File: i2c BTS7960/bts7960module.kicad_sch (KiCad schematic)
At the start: 42 parts, among them J2 Conn_01x04, J5 jst, U10 BTS7960B, U11 BTS7960B, U7 74AHC244, U8 BTS7960B, U9 BTS7960B

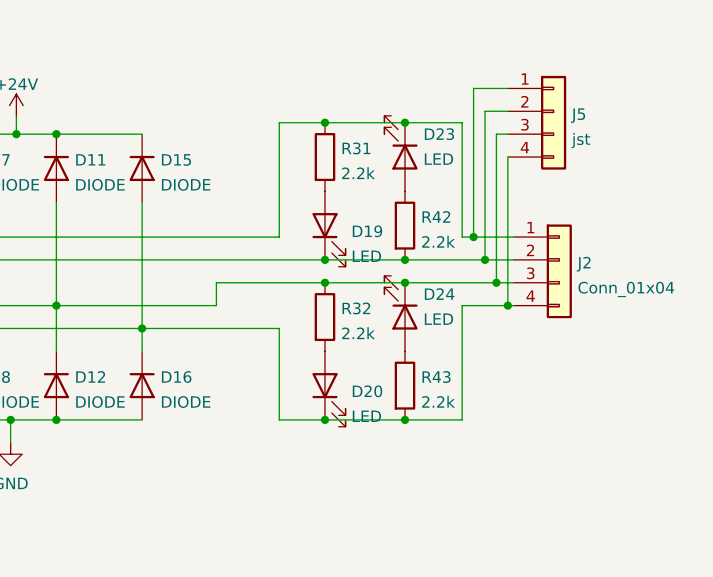
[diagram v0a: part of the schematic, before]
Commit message: tweaked buck converter hole sizes and silk
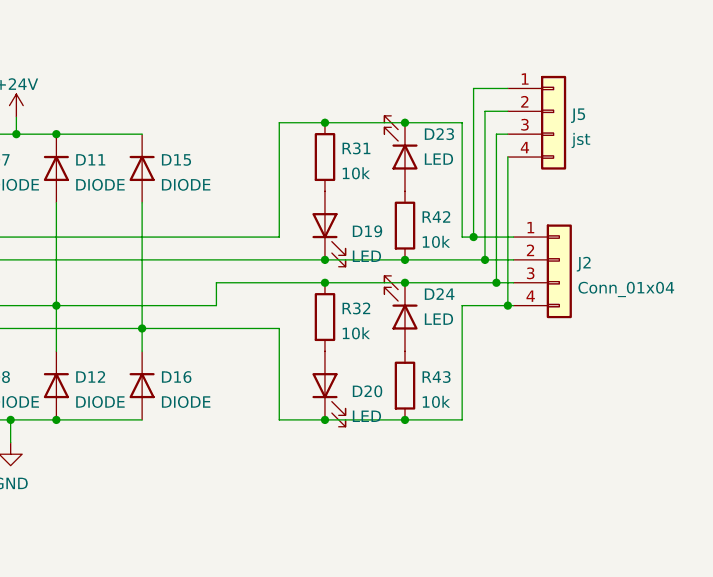
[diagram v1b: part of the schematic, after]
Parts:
- R31, R32, R42, R43: value 2.2k -> 10k
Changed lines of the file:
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@@
       (effects (font (size 1.27 1.27)) (justify left))
     )
-    (property "Value" "2.2k" (id 1) (at 244.348 91.4016 0)
+    (property "Value" "10k" (id 1) (at 244.348 91.4016 0)
       (effects (font (size 1.27 1.27)) (justify left))
     )
@@
       (effects (font (size 1.27 1.27)) (justify left))
     )
-    (property "Value" "2.2k" (id 1) (at 253.238 116.8016 0)
+    (property "Value" "10k" (id 1) (at 253.238 116.8016 0)
       (effects (font (size 1.27 1.27)) (justify left))
     )
@@
       (effects (font (size 1.27 1.27)) (justify left))
     )
-    (property "Value" "2.2k" (id 1) (at 253.238 99.0216 0)
+    (property "Value" "10k" (id 1) (at 253.238 99.0216 0)
       (effects (font (size 1.27 1.27)) (justify left))
     )
@@
       (effects (font (size 1.27 1.27)) (justify left))
     )
-    (property "Value" "2.2k" (id 1) (at 244.348 109.1816 0)
-      (effects (font (size 1.27 1.27)) (justify left))
-    )
+    (property "Value" "10k" (id 1) (at 244.348 109.1816 0)
+      (effects (font (size 1.27 1.27)) (justify left))
+    )

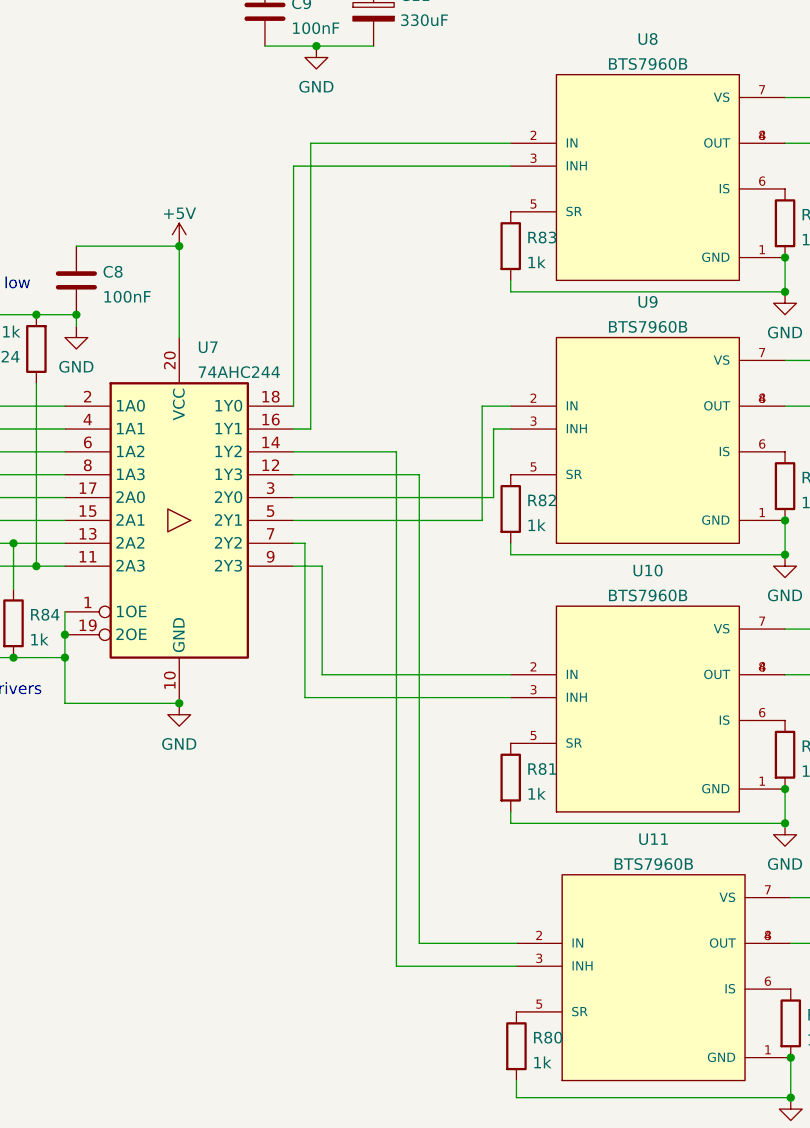
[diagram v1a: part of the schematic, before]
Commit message: reel detent added
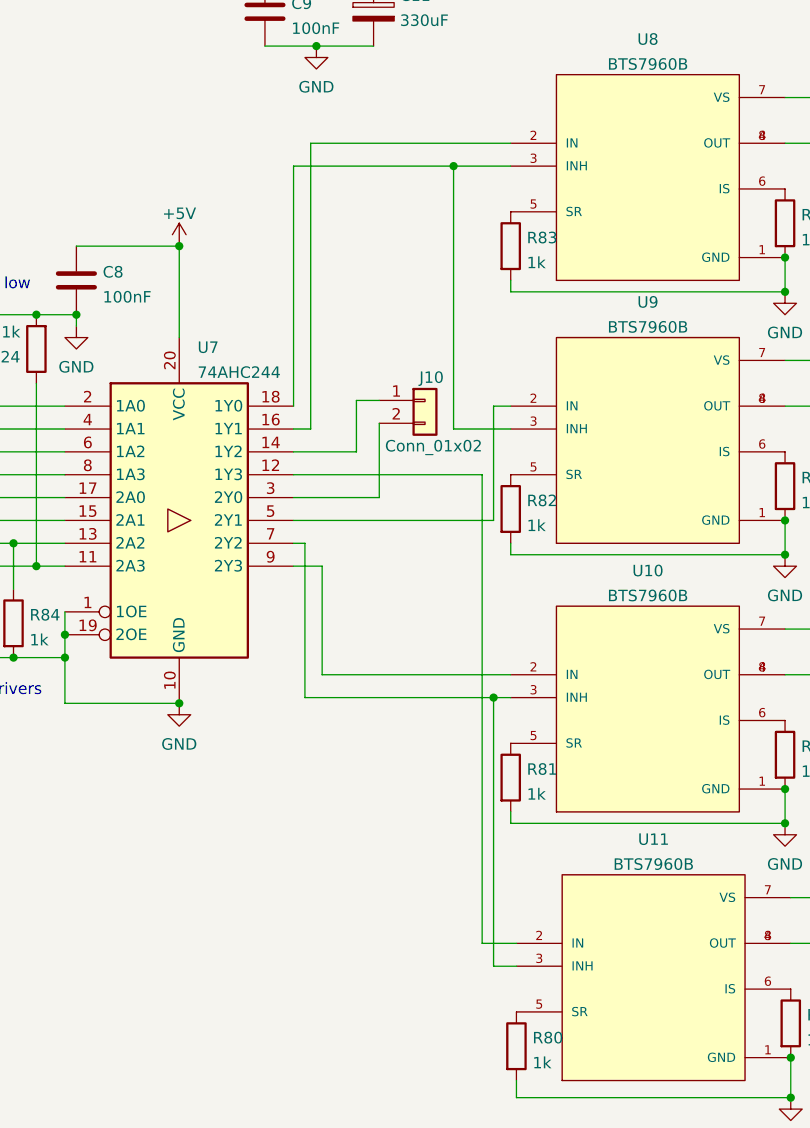
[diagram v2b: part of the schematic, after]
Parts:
- added J10: Conn_01x02, Connector_PinHeader_2.54mm:PinHeader_2x01_P2.54mm_Vertical, symbol Connector_Generic:Conn_01x02
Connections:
- net at U11.3 (INH): now also U10.3 (INH), U7.7 (2Y2); no longer U7.14 (1Y2)
- net at U9.3 (INH): now also U7.18 (1Y0), U8.3 (INH); no longer U7.3 (2Y0)
- new net: J10.1 (Pin_1), U7.14 (1Y2)
- new net: J10.2 (Pin_2), U7.3 (2Y0)
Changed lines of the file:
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@@
   (junction (at 105.41 57.785) (diameter 0) (color 0 0 0 0)
   )
+  (junction (at 140.335 107.95) (diameter 0) (color 0 0 0 0)
+  )
   (junction (at 173.355 147.955) (diameter 0) (color 0 0 0 0)
   )
@@
   (junction (at 92.71 100.965) (diameter 0) (color 0 0 0 0)
   )
+  (junction (at 135.89 48.895) (diameter 0) (color 0 0 0 0)
+  )
   (junction (at 203.2 100.965) (diameter 0) (color 0 0 0 0)
   )
@@
     (stroke (width 0) (type default) (color 0 0 0 0))
   )
-  (wire (pts (xy 139.065 75.565) (xy 139.065 88.265))
+  (wire (pts (xy 140.335 75.565) (xy 140.335 88.265))
     (stroke (width 0) (type default) (color 0 0 0 0))
   )
@@
     (stroke (width 0) (type default) (color 0 0 0 0))
   )
+  (wire (pts (xy 118.11 80.645) (xy 125.095 80.645))
+    (stroke (width 0) (type default) (color 0 0 0 0))
+  )
   (wire (pts (xy 93.98 65.405) (xy 93.98 66.675))
     (stroke (width 0) (type default) (color 0 0 0 0))
@@
     (stroke (width 0) (type default) (color 0 0 0 0))
   )
-  (wire (pts (xy 129.54 80.645) (xy 129.54 137.795))
-    (stroke (width 0) (type default) (color 0 0 0 0))
-  )
   (wire (pts (xy 203.2 118.745) (xy 207.645 118.745))
     (stroke (width 0) (type default) (color 0 0 0 0))
@@
     (stroke (width 0) (type default) (color 0 0 0 0))
   )
-  (wire (pts (xy 118.11 80.645) (xy 129.54 80.645))
-    (stroke (width 0) (type default) (color 0 0 0 0))
-  )
   (wire (pts (xy 68.58 78.105) (xy 92.71 78.105))
     (stroke (width 0) (type default) (color 0 0 0 0))
@@
     (stroke (width 0) (type default) (color 0 0 0 0))
   )
+  (wire (pts (xy 127.635 77.47) (xy 127.635 85.725))
+    (stroke (width 0) (type default) (color 0 0 0 0))
+  )
+  (wire (pts (xy 125.095 74.93) (xy 127.635 74.93))
+    (stroke (width 0) (type default) (color 0 0 0 0))
+  )
   (wire (pts (xy 180.975 41.275) (xy 180.975 70.485))
     (stroke (width 0) (type default) (color 0 0 0 0))
@@
     (stroke (width 0) (type default) (color 0 0 0 0))
   )
-  (wire (pts (xy 118.11 85.725) (xy 140.335 85.725))
-    (stroke (width 0) (type default) (color 0 0 0 0))
-  )
   (wire (pts (xy 242.57 118.745) (xy 251.46 118.745))
     (stroke (width 0) (type default) (color 0 0 0 0))
@@
     (stroke (width 0) (type default) (color 0 0 0 0))
   )
+  (wire (pts (xy 127.635 85.725) (xy 118.11 85.725))
+    (stroke (width 0) (type default) (color 0 0 0 0))
+  )
   (wire (pts (xy 260.35 84.455) (xy 260.35 100.965))
     (stroke (width 0) (type default) (color 0 0 0 0))
@@
     (stroke (width 0) (type default) (color 0 0 0 0))
   )
+  (wire (pts (xy 119.38 107.95) (xy 140.335 107.95))
+    (stroke (width 0) (type default) (color 0 0 0 0))
+  )
   (wire (pts (xy 82.55 73.025) (xy 82.55 88.265))
     (stroke (width 0) (type default) (color 0 0 0 0))
@@
     (stroke (width 0) (type default) (color 0 0 0 0))
   )
+  (wire (pts (xy 140.335 137.795) (xy 140.335 107.95))
+    (stroke (width 0) (type default) (color 0 0 0 0))
+  )
   (wire (pts (xy 64.135 90.805) (xy 86.995 90.805))
     (stroke (width 0) (type default) (color 0 0 0 0))
@@
     (stroke (width 0) (type default) (color 0 0 0 0))
   )
-  (wire (pts (xy 132.08 83.185) (xy 132.08 135.255))
-    (stroke (width 0) (type default) (color 0 0 0 0))
-  )
-  (wire (pts (xy 140.335 78.105) (xy 142.24 78.105))
+  (wire (pts (xy 139.065 83.185) (xy 139.065 135.255))
+    (stroke (width 0) (type default) (color 0 0 0 0))
+  )
+  (wire (pts (xy 135.89 78.105) (xy 142.24 78.105))
     (stroke (width 0) (type default) (color 0 0 0 0))
   )
@@
     (stroke (width 0) (type default) (color 0 0 0 0))
   )
+  (wire (pts (xy 142.875 137.795) (xy 140.335 137.795))
+    (stroke (width 0) (type default) (color 0 0 0 0))
+  )
   (wire (pts (xy 120.015 78.105) (xy 120.015 46.355))
     (stroke (width 0) (type default) (color 0 0 0 0))
   )
-  (wire (pts (xy 140.335 78.105) (xy 140.335 85.725))
-    (stroke (width 0) (type default) (color 0 0 0 0))
-  )
   (wire (pts (xy 114.935 35.56) (xy 120.65 35.56))
     (stroke (width 0) (type default) (color 0 0 0 0))
@@
     (stroke (width 0) (type default) (color 0 0 0 0))
   )
+  (wire (pts (xy 135.89 48.895) (xy 142.24 48.895))
+    (stroke (width 0) (type default) (color 0 0 0 0))
+  )
   (wire (pts (xy 86.995 90.805) (xy 92.71 90.805))
     (stroke (width 0) (type default) (color 0 0 0 0))
@@
     (stroke (width 0) (type default) (color 0 0 0 0))
   )
-  (wire (pts (xy 139.065 88.265) (xy 118.11 88.265))
+  (wire (pts (xy 125.095 80.645) (xy 125.095 74.93))
+    (stroke (width 0) (type default) (color 0 0 0 0))
+  )
+  (wire (pts (xy 140.335 88.265) (xy 118.11 88.265))
     (stroke (width 0) (type default) (color 0 0 0 0))
   )
@@
     (stroke (width 0) (type default) (color 0 0 0 0))
   )
-  (wire (pts (xy 139.065 75.565) (xy 142.24 75.565))
+  (wire (pts (xy 140.335 75.565) (xy 142.24 75.565))
     (stroke (width 0) (type default) (color 0 0 0 0))
   )
@@
     (stroke (width 0) (type default) (color 0 0 0 0))
   )
-  (wire (pts (xy 119.38 107.95) (xy 142.24 107.95))
+  (wire (pts (xy 118.11 48.895) (xy 135.89 48.895))
     (stroke (width 0) (type default) (color 0 0 0 0))
   )
@@
     (stroke (width 0) (type default) (color 0 0 0 0))
   )
-  (wire (pts (xy 118.11 48.895) (xy 142.24 48.895))
-    (stroke (width 0) (type default) (color 0 0 0 0))
-  )
-  (wire (pts (xy 129.54 137.795) (xy 142.875 137.795))
-    (stroke (width 0) (type default) (color 0 0 0 0))
-  )
-  (wire (pts (xy 132.08 135.255) (xy 142.875 135.255))
+  (wire (pts (xy 139.065 135.255) (xy 142.875 135.255))
     (stroke (width 0) (type default) (color 0 0 0 0))
   )
@@
     (stroke (width 0) (type default) (color 0 0 0 0))
   )
+  (wire (pts (xy 135.89 78.105) (xy 135.89 48.895))
+    (stroke (width 0) (type default) (color 0 0 0 0))
+  )
   (wire (pts (xy 242.57 100.965) (xy 251.46 100.965))
     (stroke (width 0) (type default) (color 0 0 0 0))
   )
-  (wire (pts (xy 118.11 83.185) (xy 132.08 83.185))
+  (wire (pts (xy 118.11 83.185) (xy 139.065 83.185))
+    (stroke (width 0) (type default) (color 0 0 0 0))
+  )
+  (wire (pts (xy 140.335 107.95) (xy 142.24 107.95))
     (stroke (width 0) (type default) (color 0 0 0 0))
   )
@@
     (pin "9")
   )
+  (symbol (lib_id "Connector_Generic:Conn_01x02") (at 132.715 74.93 0) (unit 1)
+    (in_bom yes) (on_board yes)
+    (property "Reference" "J10" (id 0) (at 132.08 72.39 0)
+      (effects (font (size 1.27 1.27)) (justify left))
+    )
+    (property "Value" "Conn_01x02" (id 1) (at 128.27 80.01 0)
+      (effects (font (size 1.27 1.27)) (justify left))
+    )
+    (property "Footprint" "Connector_PinHeader_2.54mm:PinHeader_2x01_P2.54mm_Vertical" (id 2) (at 132.715 74.93 0)
+      (effects (font (size 1.27 1.27)) hide)
+    )
+    (property "Datasheet" "~" (id 3) (at 132.715 74.93 0)
+      (effects (font (size 1.27 1.27)) hide)
+    )
+    (pin "1")
+    (pin "2")
+  )
   (symbol (lib_id "power:GND") (at 120.65 35.56 0) (unit 1)
